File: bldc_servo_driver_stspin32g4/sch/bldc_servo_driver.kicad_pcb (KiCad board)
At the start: 4 copper layers, 60 x 60 mm, 151 parts, among them IC1 STSPIN32G4, IC3 LDFMPVR, IC5 SN65HVD485EDGKR, IC6 TLT9251VLEXUMA1, J1 Conn_01x05, J2 Conn_01x04, J3 Conn_01x04, J4 52271-1179, J5 Conn_01x04, Q1 STL180N6F7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

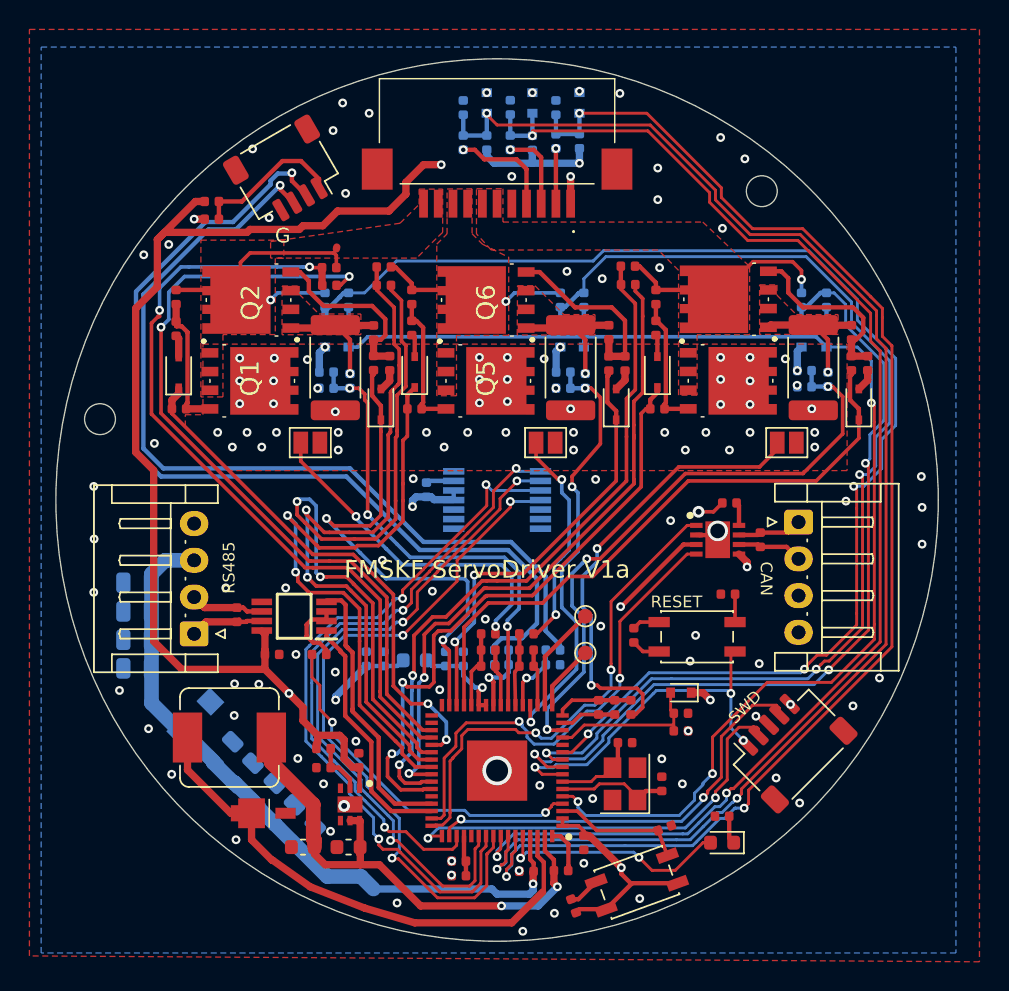
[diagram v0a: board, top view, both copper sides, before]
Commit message: fix : [G4sch] debug port FPC connector
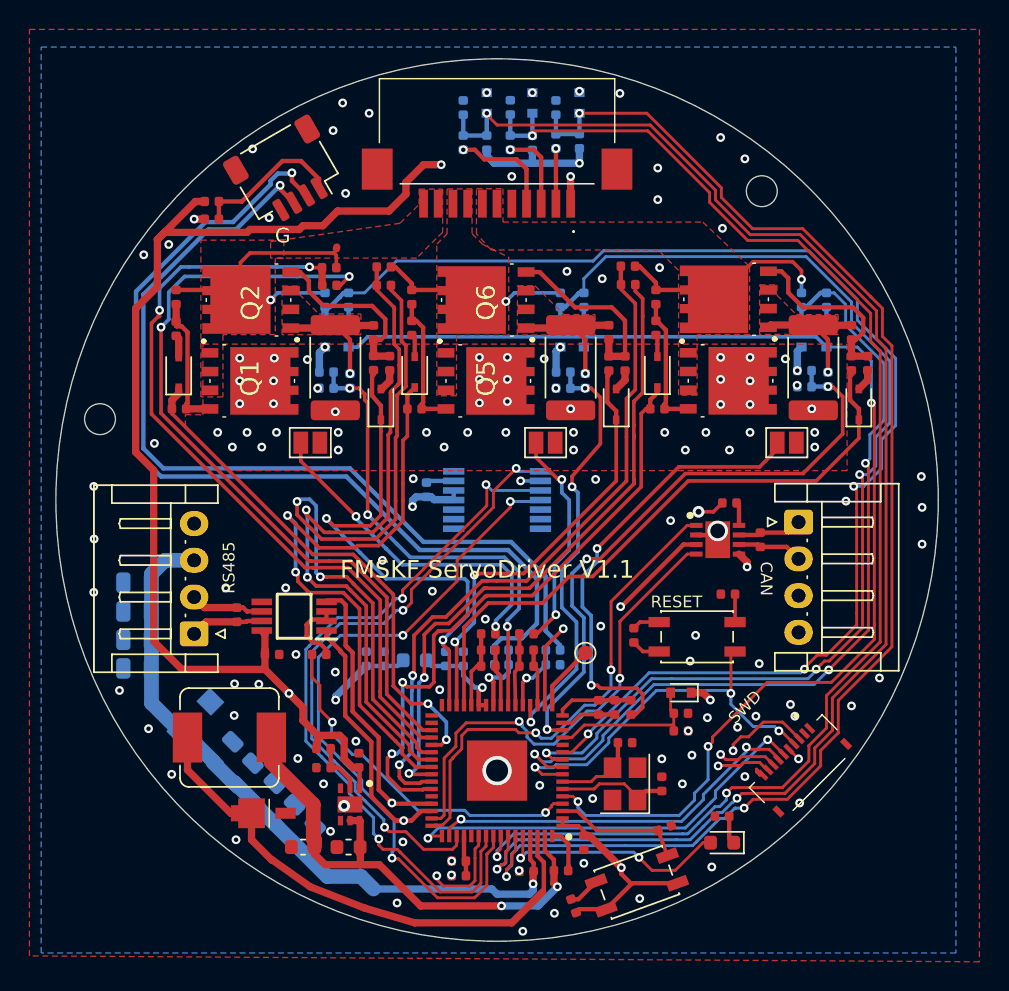
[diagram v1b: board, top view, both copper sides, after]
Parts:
- removed TP2: TestPoint, TestPoint:TestPoint_Pad_D1.0mm
- J1: value Conn_01x05 -> 1-2328702-0; footprint Connector_JST:JST_SH_SM05B-SRSS-TB_1x05-1MP_P1.00mm_Horizontal -> SamacSys_Parts:123287020
- moved J1 1.12 mm to (120.3, 117.8)
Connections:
- IC1 pad 18: /subSch_extcon/ANALOG3 -> /subSch_mcu/MCU_SPI_BUS2
- IC1 pad 54: /subSch_mcu/MCU_SPI_BUS2 -> /subSch_mcu/MCU_SWD_BUS3
- J1 pad 1: /subSch_mcu/MCU_SWD_BUS2 -> GND
- J1 pad 2: /subSch_mcu/MCU_SWD_BUS1 -> Net-(J1-Pad2)
- J1 pad 3: GND -> /subSch_mcu/MCU_SWD_BUS3
- J1 pad 4: /subSch_mcu/MCU_SWD_BUS0 -> /subSch_mcu/MCU_SWD_BUS2
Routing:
- net /subSch_mcu/MCU_SWD_BUS3: track 0.00 -> 37.9 mm, vias 0 -> 2
- net /subSch_extcon/COM_BUS3: track 18.8 -> 49.4 mm, vias 0 -> 2
- net /subSch_extcon/COM_BUS4: track 16.8 -> 46.0 mm, vias 0 -> 2
- net /subSch_mcu/MCU_SPI_BUS2: track 46.4 -> 18.6 mm, vias 3 -> 2
- net /subSch_extcon/ANALOG3: track 7.19 -> 0.00 mm
- net +3V3: track 267.5 -> 273.0 mm, vias 16 -> 17
- net /subSch_mcu/MCU_SWD_BUS0: track 28.8 -> 26.1 mm
- net /subSch_mcu/MCU_SWD_BUS2: track 26.8 -> 28.9 mm
- net /subSch_mcu/HALL_U: track 90.0 -> 91.9 mm
- net /subSch_mcu/HALL_V: track 96.0 -> 97.7 mm
- net /subSch_mcu/HALL_W: track 91.0 -> 92.4 mm
- net GND: track 3.48 -> 4.33 mm, vias 99 -> 105
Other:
- board text added: "FMSKF ServoDriver V1.1"
- board text removed: "FMSKF ServoDriver V1a"
